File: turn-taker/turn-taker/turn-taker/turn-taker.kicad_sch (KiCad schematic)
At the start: 7 parts, among them J1 Conn_01x04_Pin, SW1 SW_Push, SW2 SW_Push, SW3 SW_SPST, U1 MT3608

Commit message: schematic fixes
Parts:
- removed U1: MT3608, Package_TO_SOT_SMD:SOT-23-6, symbol Regulator_Switching:MT3608
- added J2: Conn_01x04, symbol Connector_Generic:Conn_01x04
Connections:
- net GND: now reaches A1.33 (AGND), Bat_In.2 (Pin_2), SW1.2, SW2.2
- net GND: now also J2.2 (Pin_2)
- net at A1.39 (VSYS): now also J2.3 (Pin_3)
- net at SW3.1 (A): now also J2.1 (Pin_1), J2.4 (Pin_4)
- net +5V: now reaches Bat_In.1 (Pin_1), SW3.2 (B)

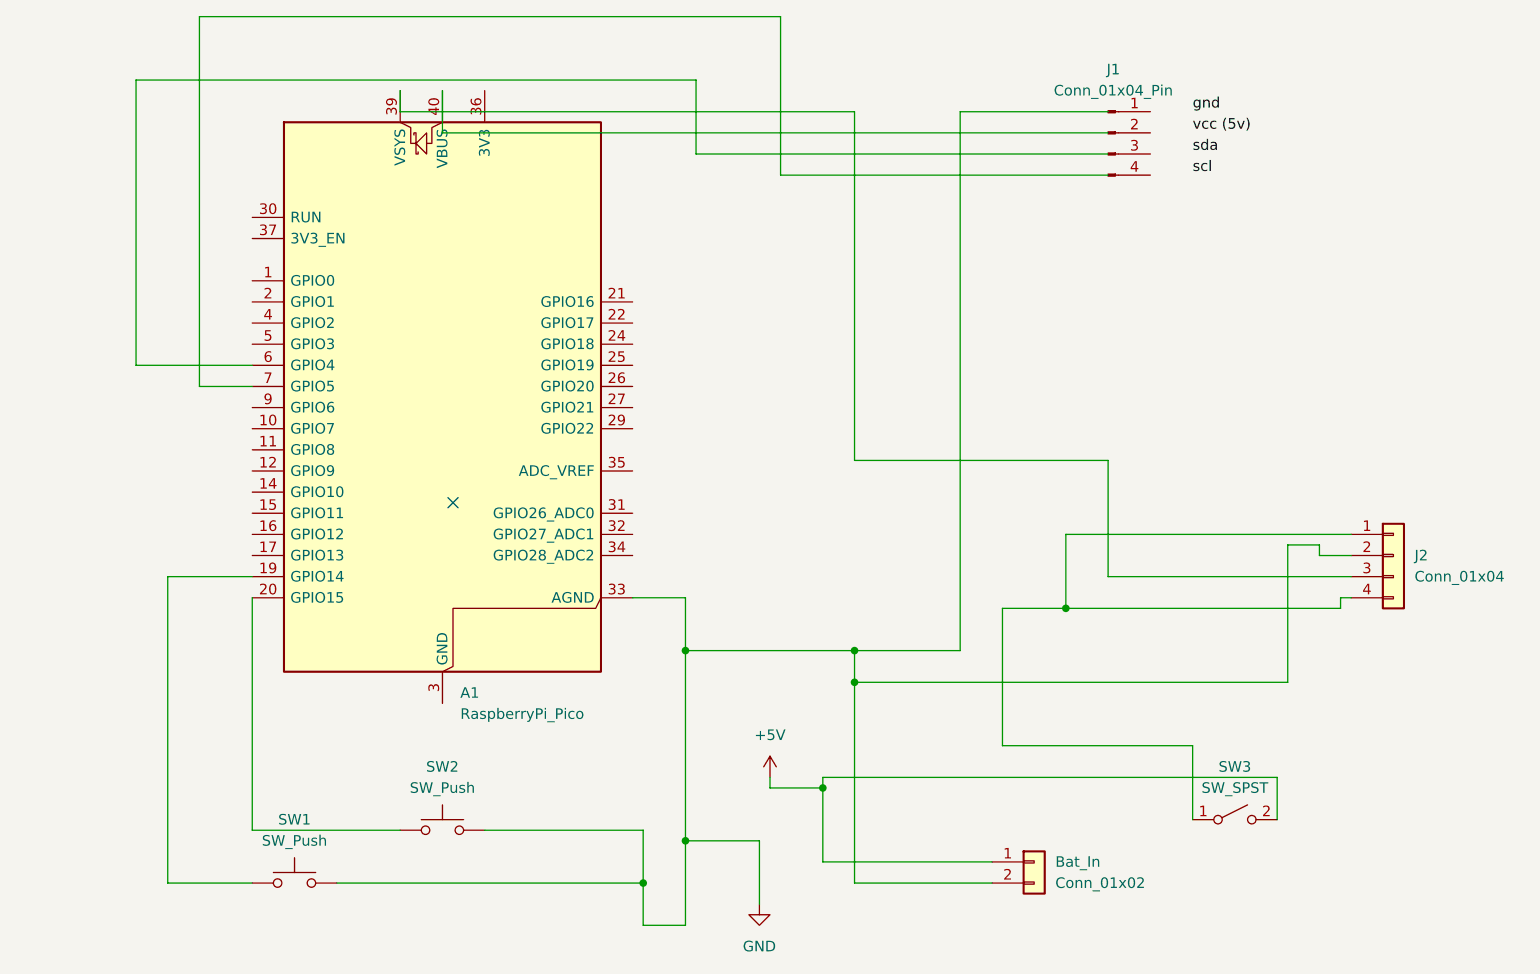
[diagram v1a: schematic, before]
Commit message: finshed the schematic with footprints
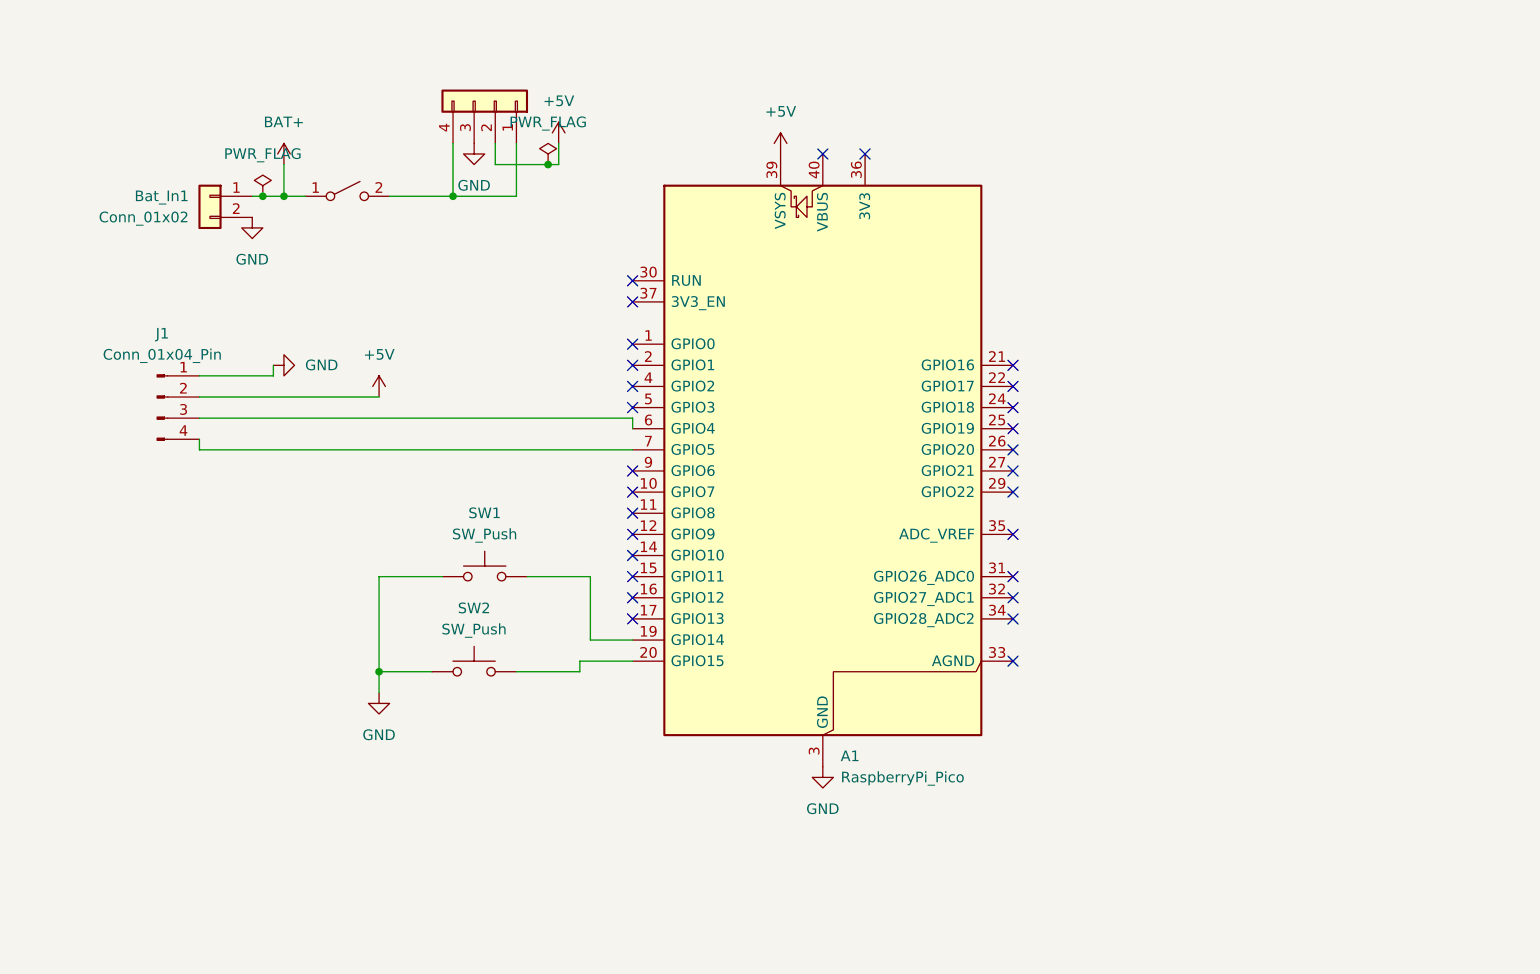
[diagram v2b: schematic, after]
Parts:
- Bat_In1: renamed from Bat_In; footprint (none) -> Connector_JST:JST_PH_S3B-PH-K_1x03_P2.00mm_Horizontal
- J1, J2: footprint (none) -> Connector_PinHeader_2.54mm:PinHeader_1x04_P2.54mm_Vertical
- SW1, SW2: footprint (none) -> Button_Switch_THT:SW_PUSH_6mm
- SW3: footprint (none) -> Button_Switch_SMD:SW_SPDT_PCM12
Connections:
- net +5V: now also A1.39 (VSYS), J1.2 (Pin_2), J2.2 (Pin_2); no longer Bat_In1.1 (Pin_1), SW3.2 (B)
- net GND: now also A1.13 (GND), A1.18 (GND), A1.23 (GND), A1.28 (GND), A1.3 (GND), A1.38 (GND), A1.8 (GND), J1.1 (Pin_1), J2.3 (Pin_3), SW1.1, SW2.1; no longer A1.33 (AGND), J2.2 (Pin_2), SW1.2, SW2.2
- net at A1.19 (GPIO14): now also SW1.2; no longer SW1.1
- net at A1.20 (GPIO15): now also SW2.2; no longer SW2.1
- net at A1.6 (GPIO4): now also J1.3 (Pin_3)
- net at A1.7 (GPIO5): now also J1.4 (Pin_4)
- net at J2.1 (Pin_1), J2.4 (Pin_4): now also SW3.2 (B); no longer SW3.1 (A)
- new net BAT+: Bat_In1.1 (Pin_1), SW3.1 (A)
- no-connect marks 1 -> 28
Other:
- moved on the sheet: A1, Bat_In1, J1, SW1, SW2

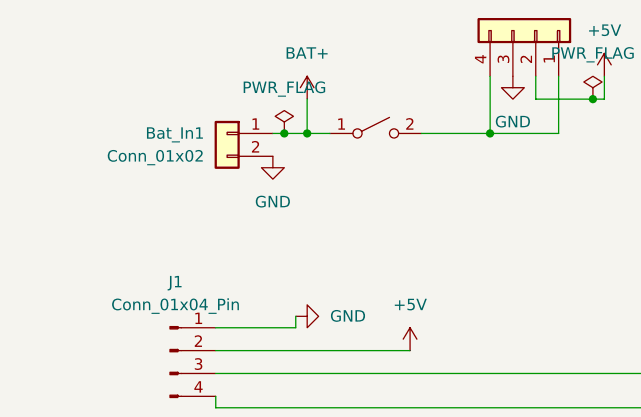
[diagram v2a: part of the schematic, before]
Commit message: fixed the switch type in the schematic to match the part
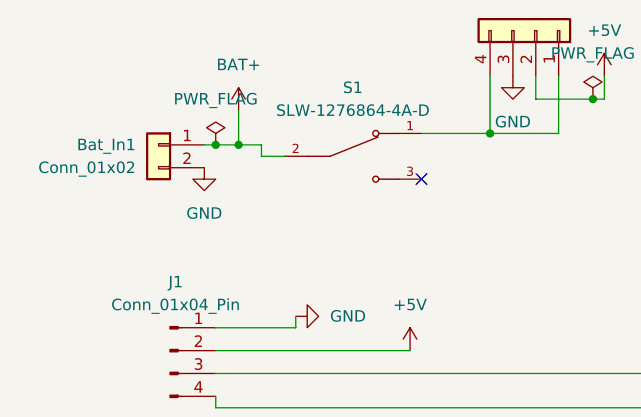
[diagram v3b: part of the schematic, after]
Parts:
- removed SW3: SW_SPST, Button_Switch_SMD:SW_SPDT_PCM12, symbol Switch:SW_SPST
- added S1: SLW-1276864-4A-D, SLW_1276864_4A_D:SW_SLW-1276864-4A-D, symbol SLW-1276864-4A-D:SLW-1276864-4A-D
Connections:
- net BAT+: now also S1.2
- net at J2.1 (Pin_1), J2.4 (Pin_4): now also S1.1
- no-connect marks 28 -> 29
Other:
- moved on the sheet: Bat_In1
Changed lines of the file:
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@@
 	)
 	(junction
-		(at 43.18 43.18)
+		(at 35.56 44.45)
 		(diameter 0)
 		(color 0 0 0 0)
@@
 	)
 	(junction
-		(at 45.72 43.18)
+		(at 38.1 44.45)
 		(diameter 0)
 		(color 0 0 0 0)
@@
 	)
 	(no_connect
+		(at 58.42 48.26)
+	)
+	(no_connect
 		(at 115.57 38.1)
 	)
@@
 	(wire
 		(pts
-			(xy 43.18 43.18) (xy 45.72 43.18)
+			(xy 35.56 44.45) (xy 38.1 44.45)
 		)
 		(stroke
@@
 	(wire
 		(pts
-			(xy 45.72 39.37) (xy 45.72 43.18)
+			(xy 38.1 40.64) (xy 38.1 44.45)
 		)
 		(stroke
@@
 	(wire
 		(pts
+			(xy 43.18 45.72) (xy 40.64 45.72)
+		)
+		(stroke
+			(width 0)
+			(type default)
+		)
+	)
+	(wire
+		(pts
+			(xy 40.64 45.72) (xy 40.64 44.45)
+		)
+		(stroke
+			(width 0)
+			(type default)
+		)
+	)
+	(wire
+		(pts
 			(xy 57.15 88.9) (xy 64.77 88.9)
 		)
@@
 	(wire
 		(pts
-			(xy 45.72 43.18) (xy 48.26 43.18)
+			(xy 38.1 44.45) (xy 40.64 44.45)
 		)
 		(stroke
@@
 	(wire
 		(pts
-			(xy 41.91 43.18) (xy 43.18 43.18)
+			(xy 34.29 44.45) (xy 35.56 44.45)
 		)
 		(stroke
@@
 	(symbol
 		(lib_id "power:GND")
-		(at 41.91 45.72 0)
+		(at 34.29 46.99 0)
 		(unit 1)
 		(exclude_from_sim no)
@@
 		(fields_autoplaced yes)
 		(property "Reference" "#PWR06"
-			(at 41.91 52.07 0)
+			(at 34.29 53.34 0)
 			(effects
 				(font
@@
 		)
 		(property "Value" "GND"
-			(at 41.91 50.8 0)
+			(at 34.29 52.07 0)
 			(effects
 				(font
@@
 		)
 		(property "Footprint" ""
-			(at 41.91 45.72 0)
+			(at 34.29 46.99 0)
 			(effects
 				(font
@@
 		)
 		(property "Datasheet" ""
-			(at 41.91 45.72 0)
+			(at 34.29 46.99 0)
 			(effects
 				(font
@@
 		)
 		(property "Description" "Power symbol creates a global label with name \"GND\" , ground"
-			(at 41.91 45.72 0)
+			(at 34.29 46.99 0)
 			(effects
 				(font
@@
 	(symbol
 		(lib_id "Connector_Generic:Conn_01x02")
-		(at 36.83 43.18 0)
+		(at 29.21 44.45 0)
 		(mirror y)
 		(unit 1)
@@
 		(dnp no)
 		(property "Reference" "Bat_In1"
-			(at 34.29 43.1799 0)
+			(at 26.67 44.4499 0)
 			(effects
 				(font
@@
 		)
 		(property "Value" "Conn_01x02"
-			(at 34.29 45.7199 0)
+			(at 26.67 46.9899 0)
 			(effects
 				(font
@@
 		)
 		(property "Footprint" "Connector_JST:JST_PH_S3B-PH-K_1x03_P2.00mm_Horizontal"
-			(at 36.83 43.18 0)
+			(at 29.21 44.45 0)
 			(effects
 				(font
@@
 		)
 		(property "Datasheet" "~"
-			(at 36.83 43.18 0)
+			(at 29.21 44.45 0)
 			(effects
 				(font
@@
 		)
 		(property "Description" "Generic connector, single row, 01x02, script generated (kicad-library-utils/schlib/autogen/connector/)"
-			(at 36.83 43.18 0)
+			(at 29.21 44.45 0)
 			(effects
 				(font
@@
 	(symbol
 		(lib_id "power:+BATT")
-		(at 45.72 39.37 0)
+		(at 38.1 40.64 0)
 		(unit 1)
 		(exclude_from_sim no)
@@
 		(fields_autoplaced yes)
 		(property "Reference" "#PWR05"
-			(at 45.72 43.18 0)
+			(at 38.1 44.45 0)
 			(effects
 				(font
@@
 		)
 		(property "Value" "BAT+"
-			(at 45.72 34.29 0)
+			(at 38.1 35.56 0)
 			(effects
 				(font
@@
 		)
 		(property "Footprint" ""
-			(at 45.72 39.37 0)
+			(at 38.1 40.64 0)
 			(effects
 				(font
@@
 		)
 		(property "Datasheet" ""
-			(at 45.72 39.37 0)
+			(at 38.1 40.64 0)
 			(effects
 				(font
@@
 		)
 		(property "Description" "Power symbol creates a global label with name \"+BATT\""
-			(at 45.72 39.37 0)
+			(at 38.1 40.64 0)
 			(effects
 				(font
@@
 	(symbol
 		(lib_id "power:PWR_FLAG")
-		(at 43.18 43.18 0)
+		(at 35.56 44.45 0)
 		(unit 1)
 		(exclude_from_sim no)
@@
 		(fields_autoplaced yes)
 		(property "Reference" "#FLG03"
-			(at 43.18 41.275 0)
+			(at 35.56 42.545 0)
 			(effects
 				(font
@@
 		)
 		(property "Value" "PWR_FLAG"
-			(at 43.18 38.1 0)
+			(at 35.56 39.37 0)
 			(effects
 				(font
@@
 		)
 		(property "Footprint" ""
-			(at 43.18 43.18 0)
+			(at 35.56 44.45 0)
 			(effects
 				(font
@@
 		)
 		(property "Datasheet" "~"
-			(at 43.18 43.18 0)
+			(at 35.56 44.45 0)
 			(effects
 				(font
@@
 		)
 		(property "Description" "Special symbol for telling ERC where power comes from"
-			(at 43.18 43.18 0)
+			(at 35.56 44.45 0)
 			(effects
 				(font
@@
 				(path "/062e3508-251e-47ff-816c-4daedf774884"
 					(reference "#FLG03")
-					(unit 1)
-				)
-			)
-		)
-	)
-	(symbol
-		(lib_id "Switch:SW_SPST")
-		(at 53.34 43.18 0)
-		(unit 1)
-		(exclude_from_sim no)
-		(in_bom yes)
-		(on_board yes)
-		(dnp no)
-		(fields_autoplaced yes)
-		(property "Reference" "SW3"
-			(at 53.34 36.83 0)
-			(effects
-				(font
-					(size 1.27 1.27)
-				)
-				(hide yes)
-			)
-		)
-		(property "Value" "SW_SPST"
-			(at 53.34 39.37 0)
-			(effects
-				(font
-					(size 1.27 1.27)
-				)
-				(hide yes)
-			)
-		)
-		(property "Footprint" "Button_Switch_SMD:SW_SPDT_PCM12"
-			(at 53.34 43.18 0)
-			(effects
-				(font
-					(size 1.27 1.27)
-				)
-				(hide yes)
-			)
-		)
-		(property "Datasheet" "~"
-			(at 53.34 43.18 0)
-			(effects
-				(font
-					(size 1.27 1.27)
-				)
-				(hide yes)
-			)
-		)
-		(property "Description" "Single Pole Single Throw (SPST) switch"
-			(at 53.34 43.18 0)
-			(effects
-				(font
-					(size 1.27 1.27)
-				)
-				(hide yes)
-			)
-		)
-		(pin "2"
-		)
-		(pin "1"
-		)
-		(instances
-			(project ""
-				(path "/062e3508-251e-47ff-816c-4daedf774884"
-					(reference "SW3")
 					(unit 1)
 				)
@@
 					(unit 1)
 				)
+			)
+		)
+	)
+	(symbol
+		(lib_id "SLW-1276864-4A-D:SLW-1276864-4A-D")
+		(at 50.8 45.72 0)
+		(unit 1)
+		(exclude_from_sim no)
+		(in_bom yes)
+		(on_board yes)
+		(dnp no)
+		(fields_autoplaced yes)
+		(property "Reference" "S1"
+			(at 50.8 38.1 0)
+			(effects
+				(font
+					(size 1.27 1.27)
+				)
+			)
+		)
+		(property "Value" "SLW-1276864-4A-D"
+			(at 50.8 40.64 0)
+			(effects
+				(font
+					(size 1.27 1.27)
+				)
+			)
+		)
+		(property "Footprint" "SLW_1276864_4A_D:SW_SLW-1276864-4A-D"
+			(at 50.8 45.72 0)
+			(effects
+				(font
+					(size 1.27 1.27)
+				)
+				(justify bottom)
+				(hide yes)
+			)
+		)
+		(property "Datasheet" ""
+			(at 50.8 45.72 0)
+			(effects
+				(font
+					(size 1.27 1.27)
+				)
+				(hide yes)
+			)
+		)
+		(property "Description" ""
+			(at 50.8 45.72 0)
+			(effects
+				(font
+					(size 1.27 1.27)
+				)
+				(hide yes)
+			)
+		)
+		(property "PARTREV" "1.01"
+			(at 50.8 45.72 0)
+			(effects
+				(font
+					(size 1.27 1.27)
+				)
+				(justify bottom)
+				(hide yes)
+			)
+		)
+		(property "STANDARD" "Manufacturer Recommendations"
+			(at 50.8 45.72 0)
+			(effects
+				(font
+					(size 1.27 1.27)
+				)
+				(justify bottom)
+				(hide yes)
+			)
+		)
+		(property "MAXIMUM_PACKAGE_HEIGHT" "10.6mm"
+			(at 50.8 45.72 0)
+			(effects
+				(font
+					(size 1.27 1.27)
+				)
+				(justify bottom)
+				(hide yes)
+			)
+		)
+		(property "MANUFACTURER" "Same Sky"
+			(at 50.8 45.72 0)
+			(effects
+				(font
+					(size 1.27 1.27)
+				)
+				(justify bottom)
+				(hide yes)
+			)
+		)
+		(pin "1"
+		)
+		(pin "3"
+		)
+		(pin "2"
+		)
+		(instances
+			(project ""
+				(path "/062e3508-251e-47ff-816c-4daedf774884"
+					(reference "S1")
+					(unit 1)
+				)

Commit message: update the jst connector for the screen in the schematic, footprint, and the pcb
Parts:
- J1: footprint Connector_PinHeader_2.54mm:PinHeader_1x04_P2.54mm_Vertical -> Connector_JST:JST_PH_B4B-PH-K_1x04_P2.00mm_Vertical
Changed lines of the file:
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@@
 			)
 		)
-		(property "Footprint" "Connector_PinHeader_2.54mm:PinHeader_1x04_P2.54mm_Vertical"
+		(property "Footprint" "Connector_JST:JST_PH_B4B-PH-K_1x04_P2.00mm_Vertical"
 			(at 30.48 67.31 0)
 			(effects
